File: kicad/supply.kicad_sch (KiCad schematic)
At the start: 45 parts, among them J8 Screw_Terminal_01x03, U14 TMUX6123, U17 TMUX6123, U19 L7815, U23 L7915, U9 LM317_TO-252

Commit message: First pass at schematic for updated bidirectional clamping and output offset when the lock is turned off, no layout changes yet
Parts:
- removed C30: 10uF, Capacitor_SMD:C_1210_3225Metric, symbol Device:C
- removed C32: 22uF, Capacitor_SMD:CP_Elec_4x5.8, symbol Device:C_Polarized
- removed C33: 100nF, Capacitor_SMD:C_0805_2012Metric, symbol Device:C
- removed R18: 1k, Resistor_SMD:R_0805_2012Metric, symbol Device:R_US
- removed R25: 330, Resistor_SMD:R_0805_2012Metric, symbol Device:R_US
- removed RV2: 2k, Potentiometer_THT:Potentiometer_Bourns_3296W_Vertical, symbol Device:R_Potentiometer_US
- removed U9: LM317_TO-252, Package_TO_SOT_SMD:TO-252-2, symbol Regulator_Linear:LM317_TO-252
- added C47, C48: 1uF, Capacitor_SMD:C_0805_2012Metric, symbol Device:C
- added U34: TMUX6123, Package_SO:VSSOP-10_3x3mm_P0.5mm, symbol library_intensity_pi:TMUX6123_split
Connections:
- net +15V: now also C47.1, U34.9 (VDD)
- net -15V: now also C48.2, U34.6 (VSS)
- net GND: now also C47.2, C48.1, U34.8 (GND)
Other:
- note removed: "max Output Voltage Limit"

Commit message: Updated schematic and design
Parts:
- removed C47, C48: 1uF, Capacitor_SMD:C_0805_2012Metric, symbol Device:C
- removed U34: TMUX6123, Package_SO:VSSOP-10_3x3mm_P0.5mm, symbol library_intensity_pi:TMUX6123_split

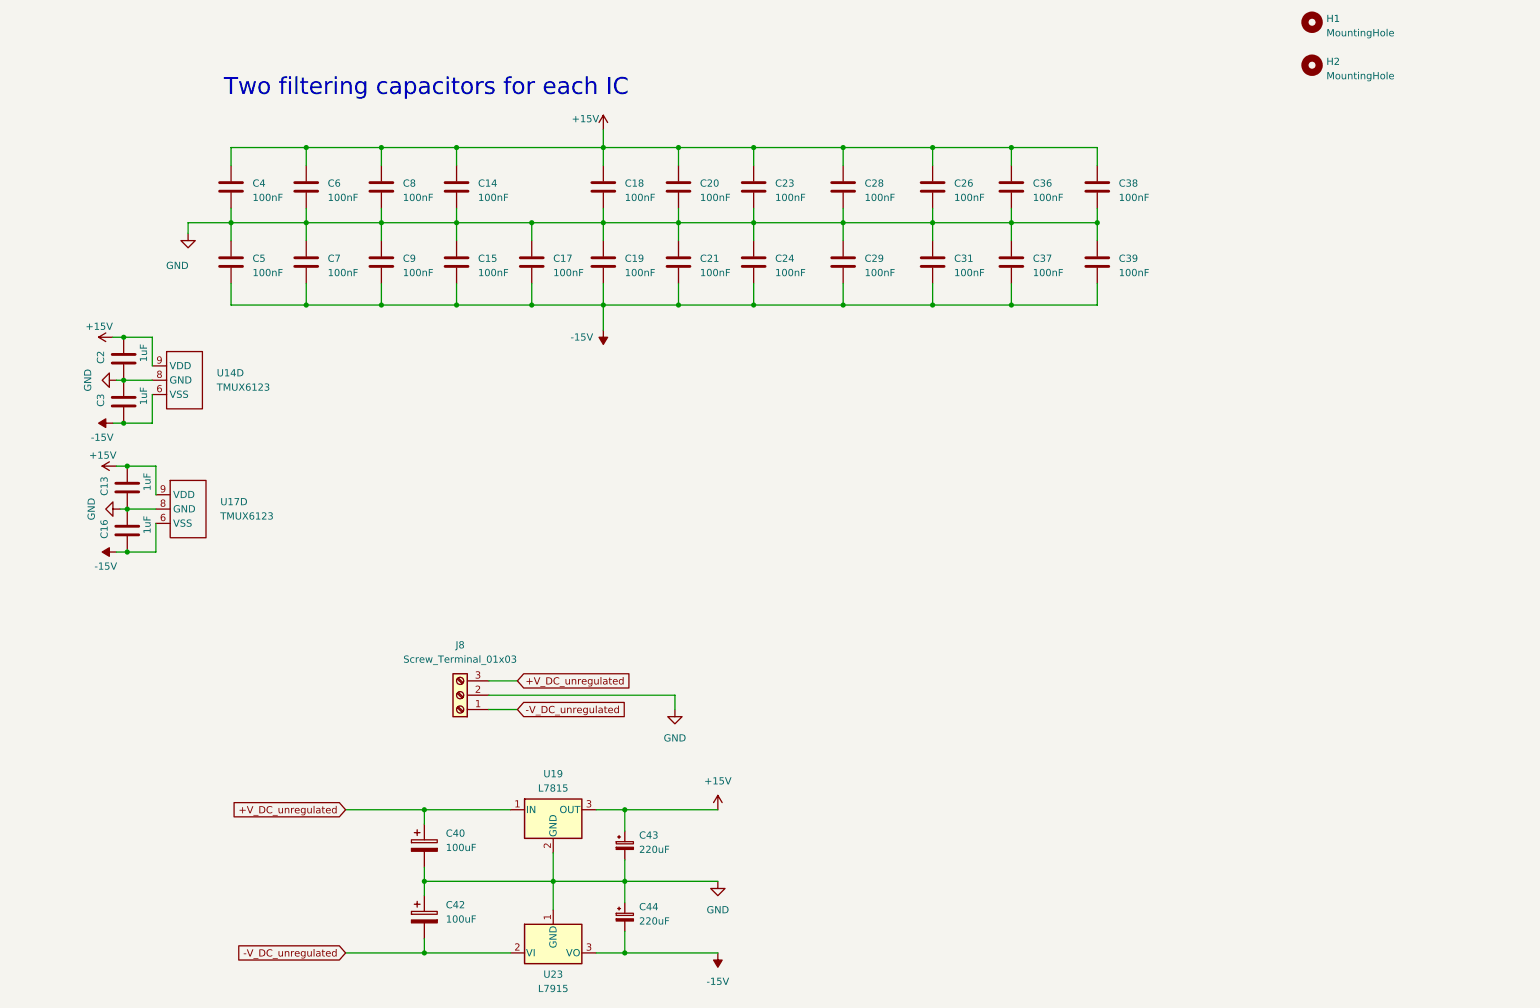
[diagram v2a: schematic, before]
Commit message: First pass at updated schematic and loose PCB grouping, TODO: Fix PI Gain values
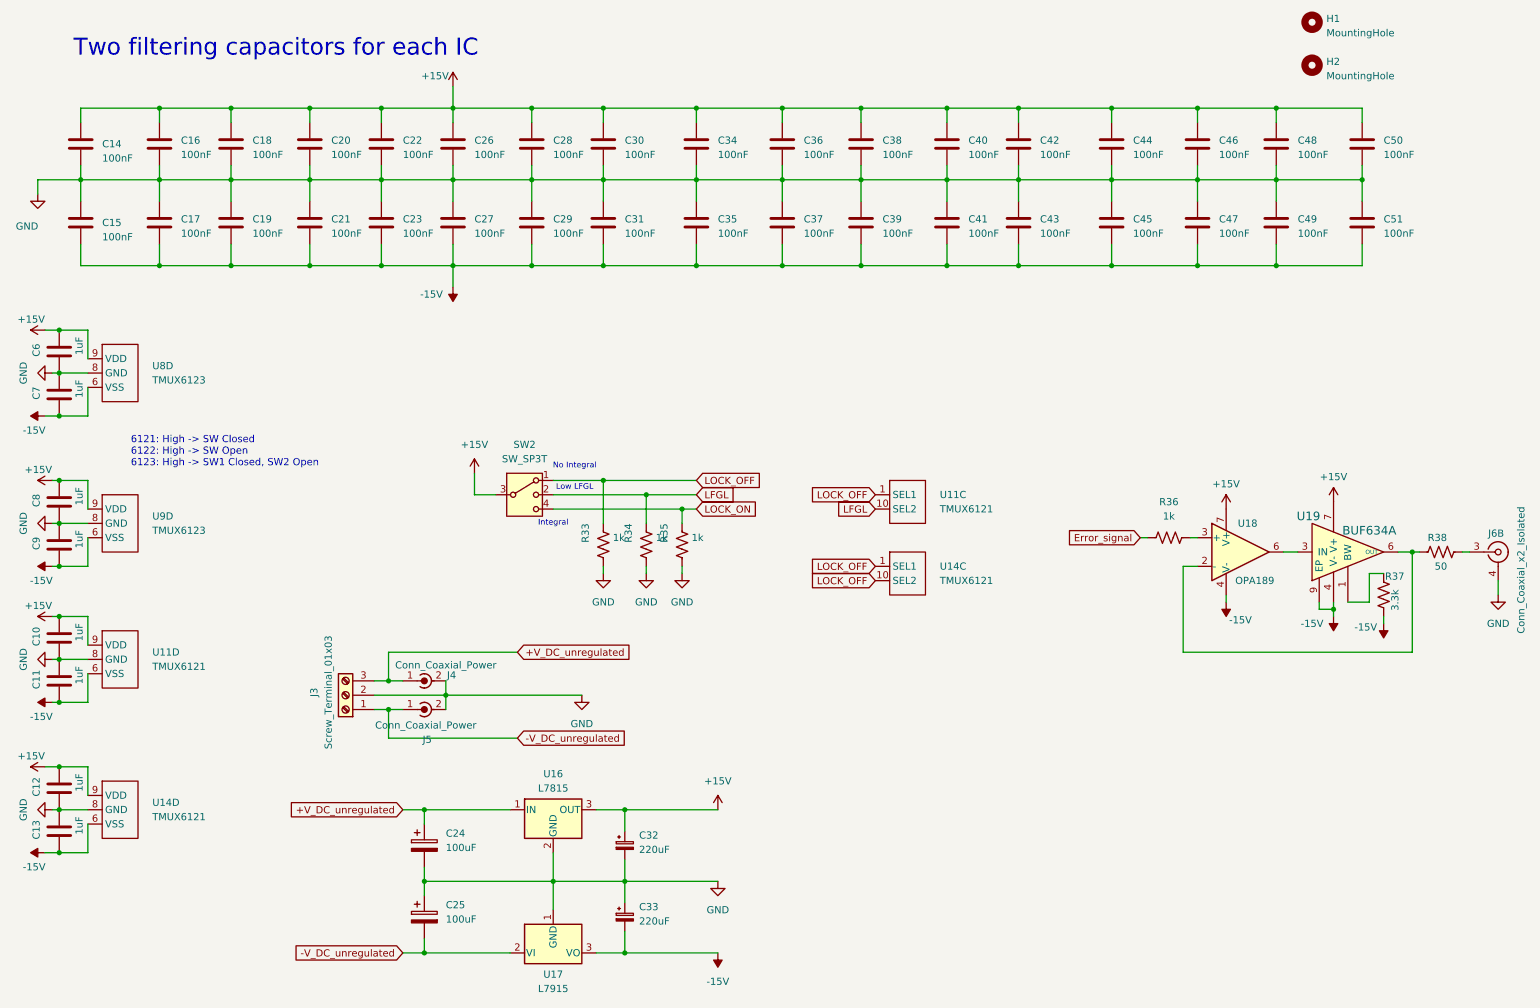
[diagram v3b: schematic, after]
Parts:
- added C10, C11, C12, C13: 1uF, Capacitor_SMD:C_0805_2012Metric, symbol Device:C
- added C22, C42, C43, C44, C45, C46, C47, C48, C49, C50, C51: 100nF, Capacitor_SMD:C_0805_2012Metric, symbol Device:C
- added J4, J5: Conn_Coaxial_Power, Connector_Coaxial:SMA_Amphenol_901-143_Horizontal, symbol Connector:Conn_Coaxial_Power
- added J6: Conn_Coaxial_x2_Isolated, Connector_Coaxial:BNC_Amphenol_031-6575_Horizontal, symbol Connector:Conn_Coaxial_x2_Isolated
- added R33, R34, R35, R36: 1k, Resistor_SMD:R_0805_2012Metric, symbol Device:R_US
- added R37: 3.3k, Resistor_SMD:R_0805_2012Metric, symbol Device:R_US
- added R38: 50, Resistor_SMD:R_0805_2012Metric, symbol Device:R_US
- added SW2: SW_SP3T, Custom_Footprints:Right Angle SP3T Vertical, symbol Switch:SW_SP3T
- added U11, U14: TMUX6121, Custom_Footprints:TMUX6121, symbol library_intensity_pi:TMUX6123_split
- added U18: OPA189, Package_SO:SOIC-8_3.9x4.9mm_P1.27mm, symbol Amplifier_Operational:OPA330xxD
- added U19: BUF634A, Custom_Footprints:BUF634AIDDAR, symbol local_lib:BUF634A
- U8: renamed from U17; footprint Package_SO:VSSOP-10_3x3mm_P0.5mm -> Custom_Footprints:TMUX6123
- U9: renamed from U14; footprint Package_SO:VSSOP-10_3x3mm_P0.5mm -> Custom_Footprints:TMUX6123
- renumbered C4 to C14, C5 to C15, C6 to C16, C7 to C17, C8 to C18, C9 to C19, C14 to C20, C15 to C21, C17 to C23, C40 to C24, C42 to C25, C18 to C26, C19 to C27, C20 to C28, C21 to C29, C23 to C30, C24 to C31, C43 to C32, C44 to C33, C28 to C34, C29 to C35, C26 to C36, C31 to C37, C36 to C38, C37 to C39, C38 to C40, C39 to C41, C13 to C6, C16 to C7, C2 to C8, C3 to C9, J8 to J3, U19 to U16, U23 to U17
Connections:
- net +15V: now also C10.1, C12.1, C22.1, C42.1, C44.1, C46.1, C48.1, C50.1, SW2.3, U11.9 (VDD), U14.9 (VDD), U18.7 (V+), U19.7 (V+)
- net +V_DC_unregulated: now also J4.1 (In)
- net -15V: now also C11.2, C13.2, C43.2, C45.2, C47.2, C49.2, C51.2, R37.1, U11.6 (VSS), U14.6 (VSS), U18.4 (V-), U19.4 (V-), U19.9 (EP)
- net -V_DC_unregulated: now also J5.1 (In)
- net GND: now also C10.2, C11.1, C12.2, C13.1, C22.2, C42.2, C43.1, C44.2, C45.1, C46.2, C47.1, C48.2, C49.1, C50.2, C51.1, J4.2 (Ext), J5.2 (Ext), J6.4 (Ext2), R33.2, R34.2, R35.2, U11.8 (GND), U14.8 (GND)
- new net: J6.3 (In2), R38.2
- new net: R37.2, U19.1 (BW)
- new net: U18.6, U19.3 (IN)
- new net: R38.1, U18.2 (-), U19.6 (OUT)
- new net: R36.1, U18.3 (+)
- new net Error_signal: R36.2
- new net LFGL: R34.1, SW2.2, U11.10 (SEL2)
- new net LOCK_OFF: R33.1, SW2.1, U11.1 (SEL1), U14.1 (SEL1), U14.10 (SEL2)
- new net LOCK_ON: R35.1, SW2.4
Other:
- note added: "6121: High -> SW Closed 6122: High -> SW Open 6123: High -> SW1 Closed, SW2 Open"
- note added: "Integral"
- note added: "Low LFGL"
- note added: "No Integral"
- moved on the sheet: C14, C15, C16, C17, C18, C19, C20, C21, C23, C26, C27, C28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
